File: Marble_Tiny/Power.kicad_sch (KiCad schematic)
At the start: 73 parts, among them J10 Barrel_Jack_Switch, Q4 DMP3013SFV, U10 TPSM863257RDXR, U11 TPSM863257RDXR, U18 TLV77325PDBVR, U20 RT9045AGSP / AP2303, U23 NCV59801CML120TCG, U24 SN74LVC1G07DBV, U25 SN74LVC1G07DBV, U4 TPSM863257RDXR, U5 TPSM863257RDXR, U6 TPSM863257RDXR

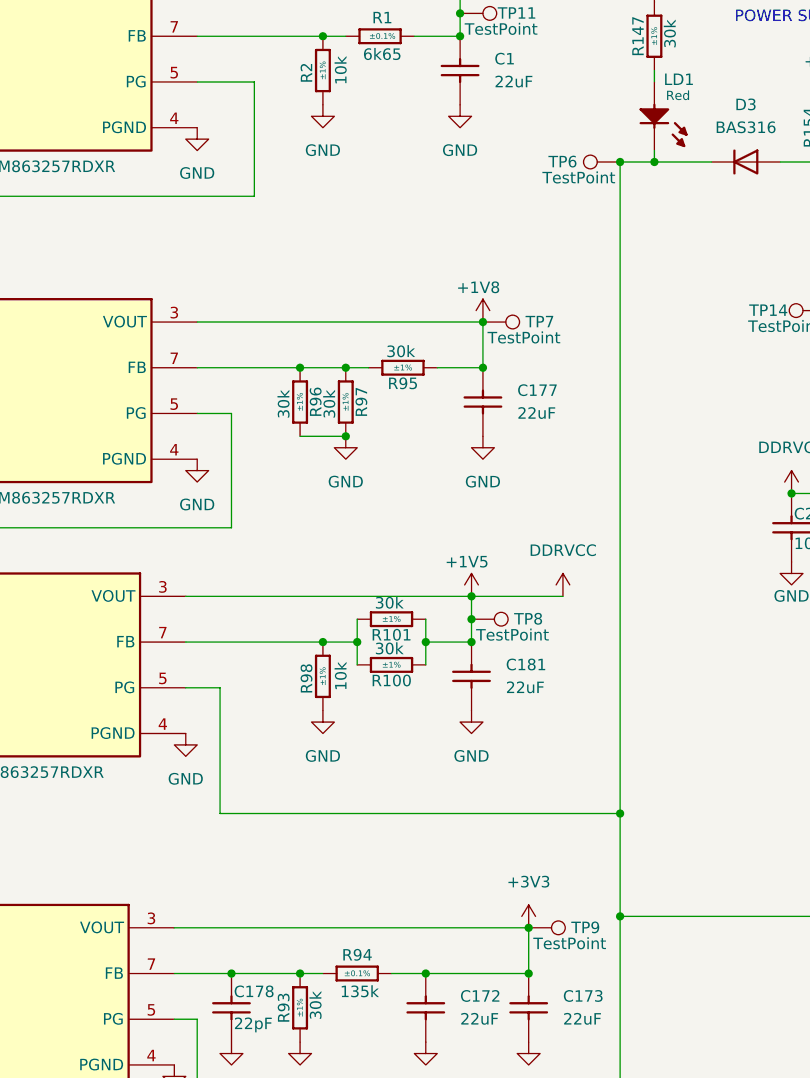
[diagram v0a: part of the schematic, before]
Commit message: connected more address lines to DDR, new board name
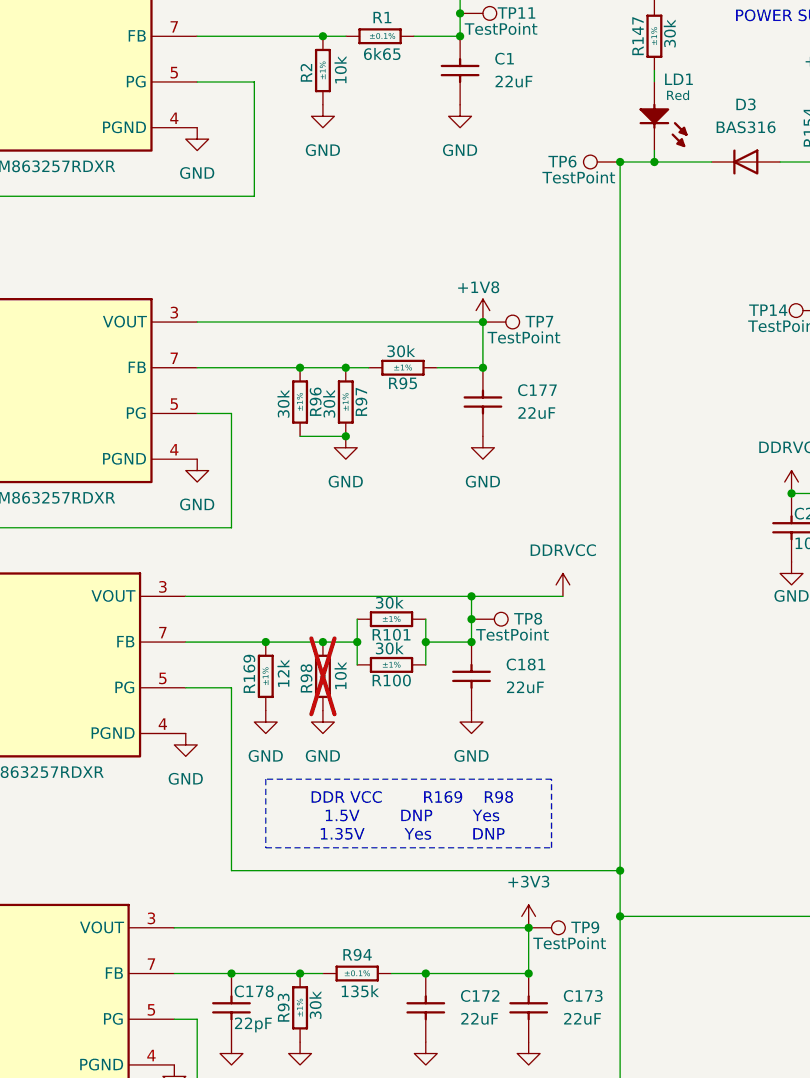
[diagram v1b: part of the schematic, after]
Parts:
- added R169: R0402_12K_1%_0.0625W_100PPM, Resistors SMD:RESC1005X40N, symbol Resistors SMD:R0402_12K_1%_0.0625W_100PPM
- R98: now not fitted
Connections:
- net GND: now also R169.1
- net at R100.1, R101.1, R98.2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: now also R169.2
- net +1V5 renamed DDRVCC
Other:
- note added: "DDR VCC R169 R98 1.5V DNP Yes 1.35V Yes DNP"

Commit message: ready for the final review
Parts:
- removed R142, R143, R144, R145, R146: R0402_4K7_1%_0.0625W_100PPM, Resistors SMD:RESC1005X40N, symbol Resistors SMD:R0402_4K7_1%_0.0625W_100PPM
- added R142, R143, R144, R145, R146: R0402_30K_1%_0.0625W_100PPM, Resistors SMD:RESC1005X40N, symbol Resistors SMD:R0402_30K_1%_0.0625W_100PPM
- added R177, R178, R179, R180, R181: R0402_12K_1%_0.0625W_100PPM, Resistors SMD:RESC1005X40N, symbol Resistors SMD:R0402_12K_1%_0.0625W_100PPM
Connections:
- net +12V: now also R142.2, R143.2, R144.2, R145.2, R146.2
- net GND: now also R177.1, R178.1, R179.1, R180.1, R181.1
- net at U10.6 (EN), U11.6 (EN), U5.5 (PG): now also R144.1, R145.1, R179.2, R180.2
- net at U4.5 (PG), U5.6 (EN): now also R143.1, R178.2
- net at U10.5 (PG), U6.6 (EN): now also R146.1, R181.2
- net at U4.6 (EN): now also R142.1, R177.2
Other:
- note added: "DDR VCC R169 R98 1.5V DNP Yes -> 1.35V Yes DNP"
- note removed: "DDR VCC R169 R98 1.5V DNP Yes 1.35V Yes DNP"
- moved on the sheet: C223
